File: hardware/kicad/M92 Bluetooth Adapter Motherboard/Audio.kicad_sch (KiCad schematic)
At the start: 32 parts, among them IC10 NJU7031D, IC5 NJU7031D, IC6 MAX4619CSE+, IC7 MCP4151-103E/SN, IC8 INA105KU/2K5G4, IC9 INA105KU/2K5G4, J3 Conn_External_Mic, Q1 PN2222ATA

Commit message: Update battery voltage divider to use larger resistor values
Increase voltage divider resistor values to reduce current draw.  Since I am never switching ADC input pins on the MCU and sampling rate is very low (once per 5 seconds), the very high impedance does not appear to impact ADC reading accuracy. I also found that the 10nF capacitor was unnecessary, so that is now removed.

Also updated JLCPCB part numbers for several resistors and capacitors to use "basic" parts instead of "extended" parts.
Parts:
- C1, C2, C3: JLCPCB Part # C5137650 -> C24497
- C1: JLCPCB Part # C5137623 -> C1846
- C3: JLCPCB Part # C5137603 -> C1848
- R1: JLCPCB Part # C102060 -> C4410
- R3, R4: JLCPCB Part # C212480 -> C17900
- R5: JLCPCB Part # C104597 -> C17927
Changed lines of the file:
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@@
       (effects (font (size 1.27 1.27)) hide)
     )
-    (property "JLCPCB Part #" "C5137650" (at 204.47 102.87 0)
+    (property "JLCPCB Part #" "C24497" (at 204.47 102.87 0)
       (effects (font (size 1.27 1.27)) hide)
     )
@@
       (effects (font (size 1.27 1.27)) hide)
     )
-    (property "JLCPCB Part #" "C212480" (at 193.04 24.13 0)
+    (property "JLCPCB Part #" "C17900" (at 193.04 24.13 0)
       (effects (font (size 1.27 1.27)) hide)
     )
@@
       (effects (font (size 1.27 1.27)) hide)
     )
-    (property "JLCPCB Part #" "C5137603" (at 86.36 40.64 0)
+    (property "JLCPCB Part #" "C1848" (at 86.36 40.64 0)
       (effects (font (size 1.27 1.27)) hide)
     )
@@
       (effects (font (size 1.27 1.27)) hide)
     )
-    (property "JLCPCB Part #" "C5137650" (at 59.69 162.56 0)
+    (property "JLCPCB Part #" "C24497" (at 59.69 162.56 0)
       (effects (font (size 1.27 1.27)) hide)
     )
@@
       (effects (font (size 1.27 1.27)) hide)
     )
-    (property "JLCPCB Part #" "C5137650" (at 76.2 92.71 0)
+    (property "JLCPCB Part #" "C24497" (at 76.2 92.71 0)
       (effects (font (size 1.27 1.27)) hide)
     )
@@
       (effects (font (size 1.27 1.27)) hide)
     )
-    (property "JLCPCB Part #" "C5137650" (at 203.2 86.36 0)
+    (property "JLCPCB Part #" "C24497" (at 203.2 86.36 0)
       (effects (font (size 1.27 1.27)) hide)
     )
@@
       (effects (font (size 1.27 1.27)) hide)
     )
-    (property "JLCPCB Part #" "C212480" (at 184.15 24.13 0)
+    (property "JLCPCB Part #" "C17900" (at 184.15 24.13 0)
       (effects (font (size 1.27 1.27)) hide)
     )
@@
       (effects (font (size 1.27 1.27)) hide)
     )
-    (property "JLCPCB Part #" "C5137650" (at 99.06 57.15 0)
+    (property "JLCPCB Part #" "C24497" (at 99.06 57.15 0)
       (effects (font (size 1.27 1.27)) hide)
     )
@@
       (effects (font (size 1.27 1.27)) hide)
     )
-    (property "JLCPCB Part #" "C102060" (at 68.58 158.75 0)
+    (property "JLCPCB Part #" "C4410" (at 68.58 158.75 0)
       (effects (font (size 1.27 1.27)) hide)
     )
@@
       (effects (font (size 1.27 1.27)) hide)
     )
-    (property "JLCPCB Part #" "C212480" (at 201.93 24.13 0)
+    (property "JLCPCB Part #" "C17900" (at 201.93 24.13 0)
       (effects (font (size 1.27 1.27)) hide)
     )
@@
       (effects (font (size 1.27 1.27)) hide)
     )
-    (property "JLCPCB Part #" "C212480" (at 88.9 158.75 0)
+    (property "JLCPCB Part #" "C17900" (at 88.9 158.75 0)
       (effects (font (size 1.27 1.27)) hide)
     )
@@
       (effects (font (size 1.27 1.27)) hide)
     )
-    (property "JLCPCB Part #" "C104597" (at 68.58 100.33 0)
+    (property "JLCPCB Part #" "C17927" (at 68.58 100.33 0)
       (effects (font (size 1.27 1.27)) hide)
     )
@@
       (effects (font (size 1.27 1.27)) hide)
     )
-    (property "JLCPCB Part #" "C212480" (at 242.57 24.13 0)
+    (property "JLCPCB Part #" "C17900" (at 242.57 24.13 0)
       (effects (font (size 1.27 1.27)) hide)
     )
@@
       (effects (font (size 1.27 1.27)) hide)
     )
-    (property "JLCPCB Part #" "C5137650" (at 233.68 34.29 0)
+    (property "JLCPCB Part #" "C24497" (at 233.68 34.29 0)
       (effects (font (size 1.27 1.27)) hide)
     )
@@
       (effects (font (size 1.27 1.27)) hide)
     )
-    (property "JLCPCB Part #" "C212480" (at 78.74 158.75 0)
+    (property "JLCPCB Part #" "C17900" (at 78.74 158.75 0)
       (effects (font (size 1.27 1.27)) hide)
     )
@@
       (effects (font (size 1.27 1.27)) hide)
     )
-    (property "JLCPCB Part #" "C212480" (at 210.82 24.13 0)
+    (property "JLCPCB Part #" "C17900" (at 210.82 24.13 0)
       (effects (font (size 1.27 1.27)) hide)
     )
@@
       (effects (font (size 1.27 1.27)) hide)
     )
-    (property "JLCPCB Part #" "C5137603" (at 157.48 128.27 0)
+    (property "JLCPCB Part #" "C1848" (at 157.48 128.27 0)
       (effects (font (size 1.27 1.27)) hide)
     )
@@
       (effects (font (size 1.27 1.27)) hide)
     )
-    (property "JLCPCB Part #" "C5137650" (at 96.52 118.11 0)
+    (property "JLCPCB Part #" "C24497" (at 96.52 118.11 0)
       (effects (font (size 1.27 1.27)) hide)
     )
@@
       (effects (font (size 1.27 1.27)) hide)
     )
-    (property "JLCPCB Part #" "C5137603" (at 208.28 123.19 0)
+    (property "JLCPCB Part #" "C1848" (at 208.28 123.19 0)
       (effects (font (size 1.27 1.27)) hide)
     )
@@
       (effects (font (size 1.27 1.27)) hide)
     )
-    (property "JLCPCB Part #" "C5137623" (at 93.98 63.5 0)
+    (property "JLCPCB Part #" "C1846" (at 93.98 63.5 0)
       (effects (font (size 1.27 1.27)) hide)
     )
@@
       (effects (font (size 1.27 1.27)) hide)
     )
-    (property "JLCPCB Part #" "C5137603" (at 208.28 146.05 0)
+    (property "JLCPCB Part #" "C1848" (at 208.28 146.05 0)
       (effects (font (size 1.27 1.27)) hide)
     )
@@
       (effects (font (size 1.27 1.27)) hide)
     )
-    (property "JLCPCB Part #" "C5137603" (at 157.48 151.13 0)
-      (effects (font (size 1.27 1.27)) hide)
-    )
+    (property "JLCPCB Part #" "C1848" (at 157.48 151.13 0)
+      (effects (font (size 1.27 1.27)) hide)
+    )

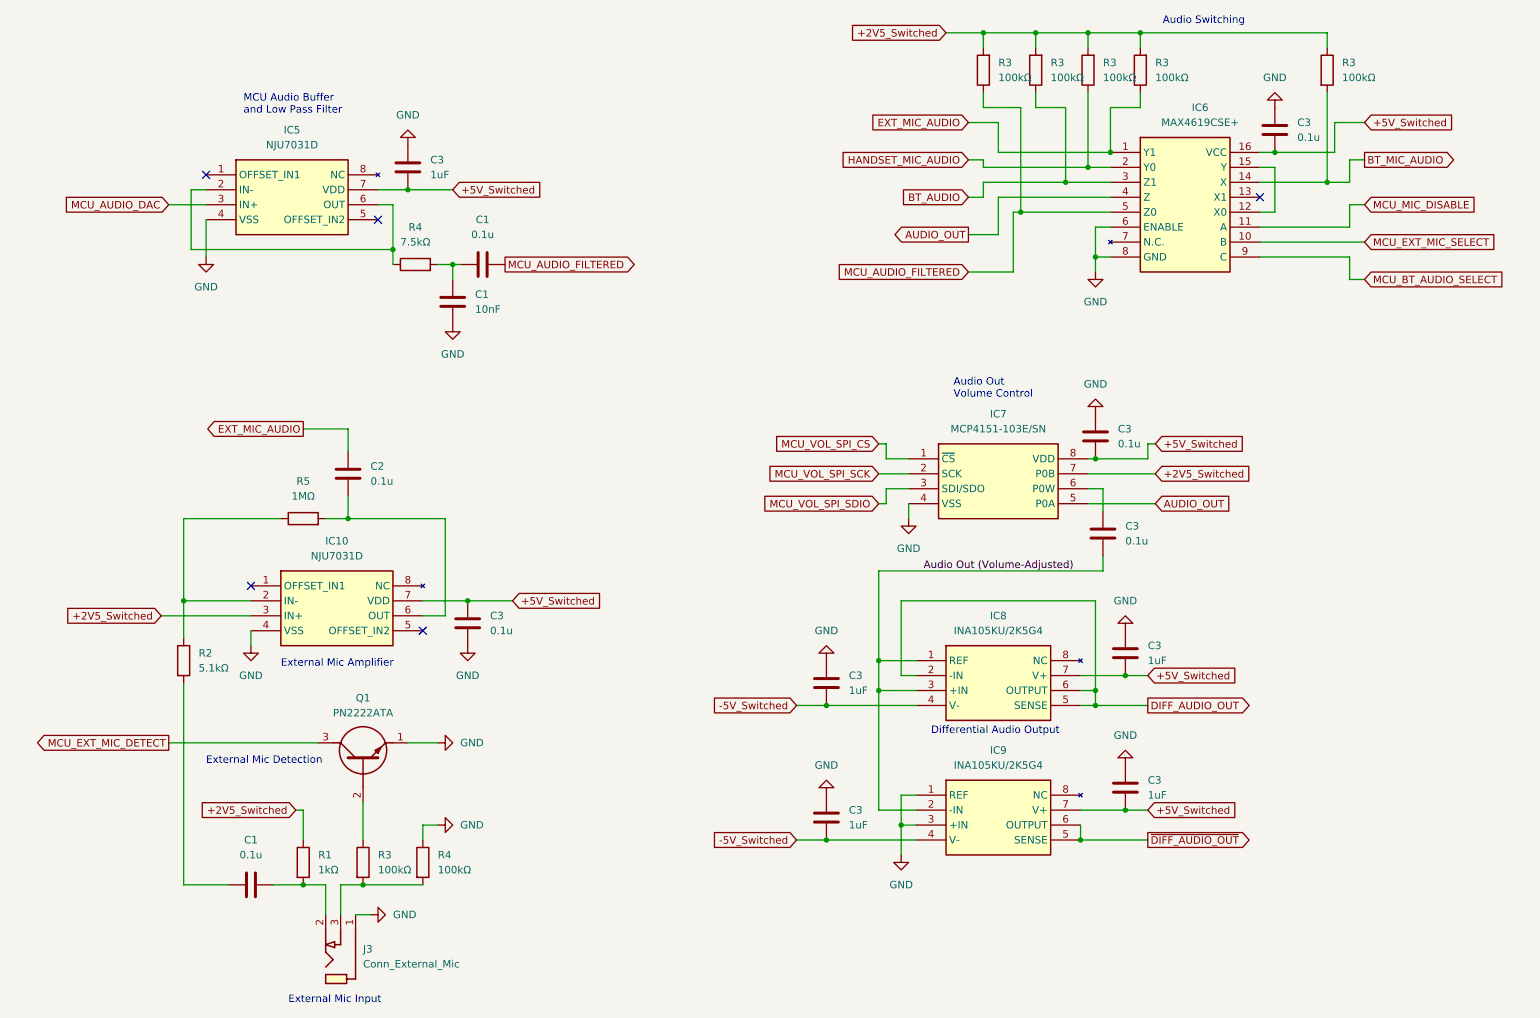
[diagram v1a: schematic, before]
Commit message: Motherboard circuit/PCB adjustments
* Add 100uf cap to stabilize the 5V power supply (reduce voltage dip during power-on of switched 5V supply).
* Add cap to 12V load switch to reduce inrush current when powering on handset.
* Part number updates to more readily available parts.
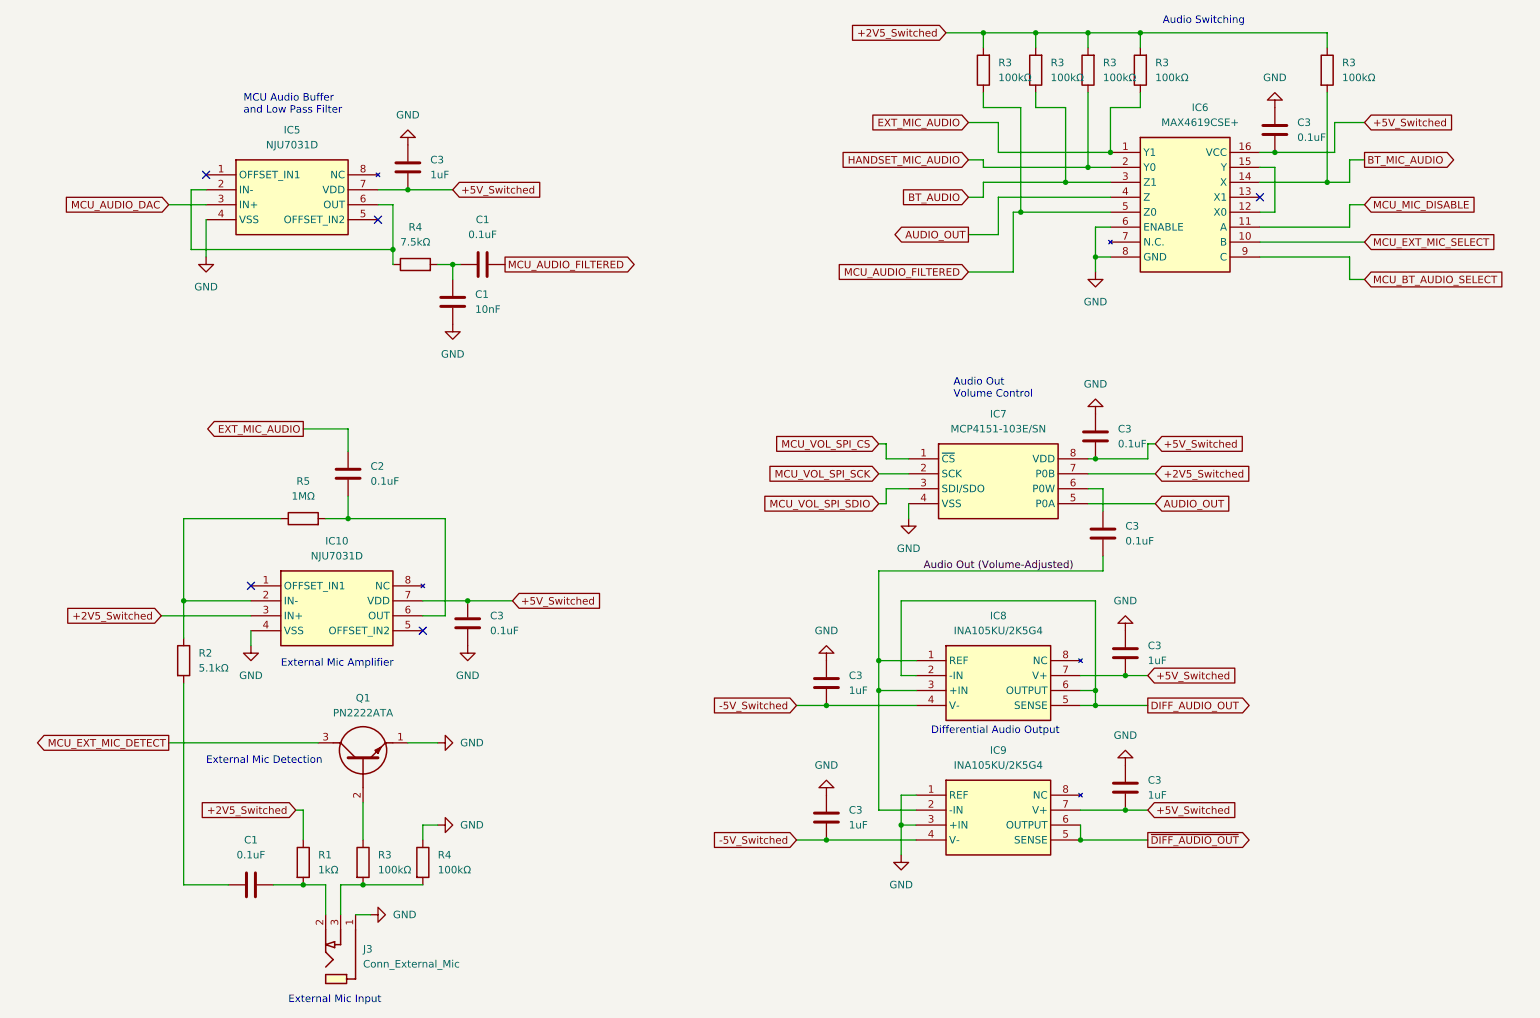
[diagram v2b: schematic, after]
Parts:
- C1, C2, C3: value 0.1u -> 0.1uF
- C1: Manufacturer_Part_Number C1206C103J4HACTU -> C1206C103J5RAC7210; Mouser Part Number 80-C1206C103J4HACTU -> 80-C1206C103J5RACLR; Mouser Price/Stock https://www.mouser.com/ProductDetail/KEMET/C1206C103J4HACTU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 -> https://www.mouser.com/ProductDetail/KEMET/C1206C103J5RAC72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
- IC6: JLCPCB Part # C1546433 -> C2673707
- R4: JLCPCB Part # C2907392 -> C465505
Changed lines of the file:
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@@
       (effects (font (size 1.27 1.27)) (justify right))
     )
-    (property "Value" "0.1u" (at 208.28 104.14 0)
+    (property "Value" "0.1uF" (at 208.28 104.14 0)
       (effects (font (size 1.27 1.27)) (justify right))
     )
@@
       (effects (font (size 1.27 1.27)))
     )
-    (property "Value" "0.1u" (at 59.69 157.48 90)
+    (property "Value" "0.1uF" (at 59.69 157.48 90)
       (effects (font (size 1.27 1.27)))
     )
@@
       (effects (font (size 1.27 1.27)) (justify left))
     )
-    (property "Value" "0.1u" (at 80.01 93.98 0)
+    (property "Value" "0.1uF" (at 80.01 93.98 0)
       (effects (font (size 1.27 1.27)) (justify left))
     )
@@
       (effects (font (size 1.27 1.27)) (justify right))
     )
-    (property "Value" "0.1u" (at 207.01 87.63 0)
+    (property "Value" "0.1uF" (at 207.01 87.63 0)
       (effects (font (size 1.27 1.27)) (justify right))
     )
@@
       (effects (font (size 1.27 1.27)) (justify left top) hide)
     )
-    (property "JLCPCB Part #" "C1546433" (at 205.74 38.1 0)
+    (property "JLCPCB Part #" "C2673707" (at 205.74 38.1 0)
       (effects (font (size 1.27 1.27)) hide)
     )
@@
       (effects (font (size 1.27 1.27)))
     )
-    (property "Value" "0.1u" (at 99.06 52.07 90)
+    (property "Value" "0.1uF" (at 99.06 52.07 90)
       (effects (font (size 1.27 1.27)))
     )
@@
       (effects (font (size 1.27 1.27)) (justify right))
     )
-    (property "Value" "0.1u" (at 237.49 35.56 0)
+    (property "Value" "0.1uF" (at 237.49 35.56 0)
       (effects (font (size 1.27 1.27)) (justify right))
     )
@@
       (effects (font (size 1.27 1.27)) (justify right))
     )
-    (property "Value" "0.1u" (at 100.33 119.38 0)
+    (property "Value" "0.1uF" (at 100.33 119.38 0)
       (effects (font (size 1.27 1.27)) (justify right))
     )
@@
       (effects (font (size 1.27 1.27)) hide)
     )
-    (property "Manufacturer_Part_Number" "C1206C103J4HACTU" (at 93.98 63.5 0)
-      (effects (font (size 1.27 1.27)) hide)
-    )
-    (property "Mouser Part Number" "80-C1206C103J4HACTU" (at 93.98 63.5 0)
-      (effects (font (size 1.27 1.27)) hide)
-    )
-    (property "Mouser Price/Stock" "https://www.mouser.com/ProductDetail/KEMET/C1206C103J4HACTU?qs=W0yvOO0ixfHuR59Cq5E7Zg%3D%3D" (at 93.98 63.5 0)
+    (property "Manufacturer_Part_Number" "C1206C103J5RAC7210" (at 93.98 63.5 0)
+      (effects (font (size 1.27 1.27)) hide)
+    )
+    (property "Mouser Part Number" "80-C1206C103J5RACLR" (at 93.98 63.5 0)
+      (effects (font (size 1.27 1.27)) hide)
+    )
+    (property "Mouser Price/Stock" "https://www.mouser.com/ProductDetail/KEMET/C1206C103J5RAC7210?qs=6%252BYqE%252B3CbMnE88U2bDOWwA%3D%3D" (at 93.98 63.5 0)
       (effects (font (size 1.27 1.27)) hide)
     )
@@
       (effects (font (size 1.27 1.27)) hide)
     )
-    (property "JLCPCB Part #" "C2907392" (at 87.63 57.15 0)
-      (effects (font (size 1.27 1.27)) hide)
-    )
+    (property "JLCPCB Part #" "C465505" (at 87.63 57.15 0)
+      (effects (font (size 1.27 1.27)) hide)
+    )

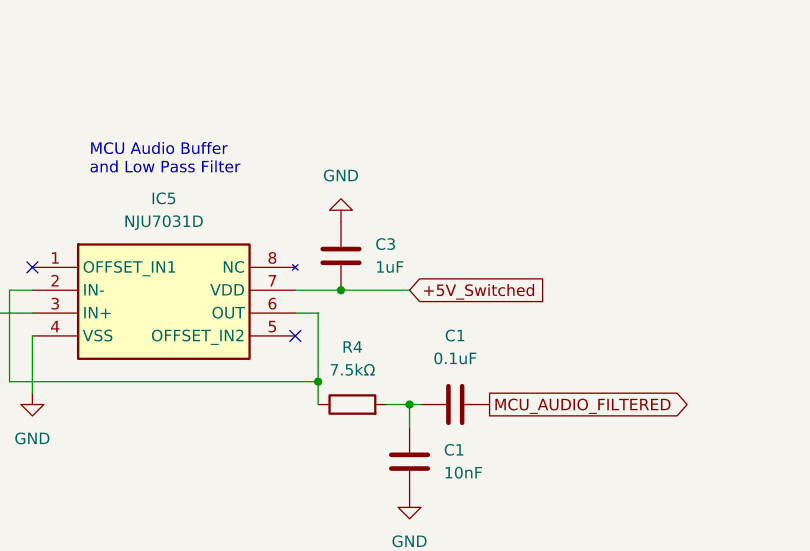
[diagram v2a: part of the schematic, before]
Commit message: Minor circuit and PCB layout adjustments
* Enable quick output discharge feature of both load switches.
* Change a decoupling cap from 1uF to 0.1uF for consistency.
* Fix incorrect labeling on the PCB of the BT module connector pinout.
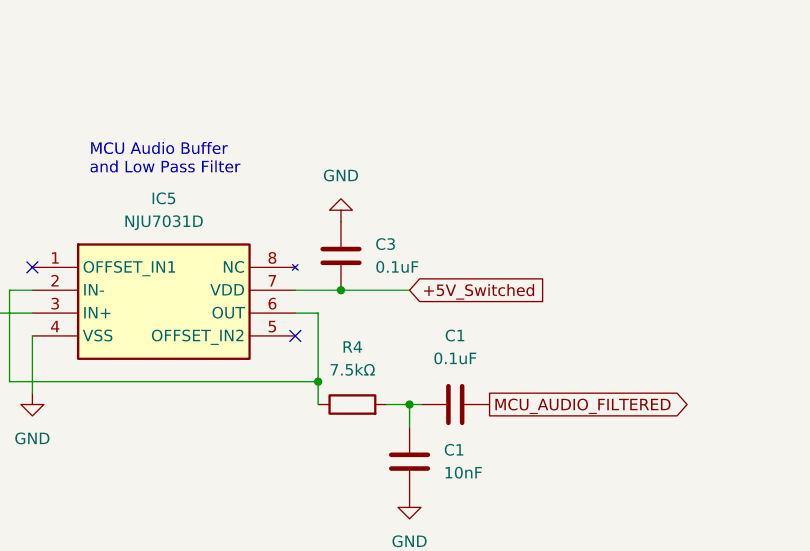
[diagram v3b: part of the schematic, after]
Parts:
- C3: value 1uF -> 0.1uF; JLCPCB Part # C1848 -> C24497; Manufacturer_Part_Number C1206C105J4RAC -> C1206C104J4HACTU; Mouser Part Number 80-C1206C105J4RAC -> 80-C1206C104J4HACTU; Mouser Price/Stock https://www.mouser.com/ProductDetail/KEMET/C1206C105J4RAC?q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 -> https://www.mouser.com/ProductDetail/KEMET/C1206C104J4HACTU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
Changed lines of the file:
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@@
       (effects (font (size 1.27 1.27)) (justify right))
     )
-    (property "Value" "1uF" (at 90.17 41.91 0)
+    (property "Value" "0.1uF" (at 90.17 41.91 0)
       (effects (font (size 1.27 1.27)) (justify right))
     )
@@
       (effects (font (size 1.27 1.27)) hide)
     )
-    (property "Manufacturer_Part_Number" "C1206C105J4RAC" (at 86.36 40.64 0)
+    (property "Manufacturer_Part_Number" "C1206C104J4HACTU" (at 86.36 40.64 0)
       (effects (font (size 1.27 1.27)) hide)
     )
-    (property "Mouser Part Number" "80-C1206C105J4RAC" (at 86.36 40.64 0)
+    (property "Mouser Part Number" "80-C1206C104J4HACTU" (at 86.36 40.64 0)
       (effects (font (size 1.27 1.27)) hide)
     )
-    (property "Mouser Price/Stock" "https://www.mouser.com/ProductDetail/KEMET/C1206C105J4RAC?qs=esDHISMOsl0f41aGH%2FVPNQ%3D%3D" (at 86.36 40.64 0)
+    (property "Mouser Price/Stock" "https://www.mouser.com/ProductDetail/KEMET/C1206C104J4HACTU?qs=W0yvOO0ixfH3SzteelzlzQ%3D%3D" (at 86.36 40.64 0)
       (effects (font (size 1.27 1.27)) hide)
     )
-    (property "JLCPCB Part #" "C1848" (at 86.36 40.64 0)
+    (property "JLCPCB Part #" "C24497" (at 86.36 40.64 0)
       (effects (font (size 1.27 1.27)) hide)
     )

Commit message: Minor schematic/pcb fixes
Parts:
- IC6: Mouser Price/Stock https://www.mouser.co.uk/ProductDetail/Analog-Devices-Maxim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 -> https://www.mouser.com/ProductDetail/Analog-Devices-Maxim-I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
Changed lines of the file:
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@@
       (effects (font (size 1.27 1.27)) (justify left top) hide)
     )
-    (property "Mouser Price/Stock" "https://www.mouser.co.uk/ProductDetail/Analog-Devices-Maxim-Integrated/MAX4619CSE%2b?qs=OjdDRS8jtCYbJC3SYTRKnA%3D%3D" (at 232.41 633.02 0)
+    (property "Mouser Price/Stock" "https://www.mouser.com/ProductDetail/Analog-Devices-Maxim-Integrated/MAX4619CSE%2b?qs=OjdDRS8jtCYbJC3SYTRKnA%3D%3D" (at 232.41 633.02 0)
       (effects (font (size 1.27 1.27)) (justify left top) hide)
     )
